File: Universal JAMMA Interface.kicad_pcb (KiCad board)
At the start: 2 copper layers, 111 x 60.8 mm, 31 parts, among them U1 LM386, U2 DIP-14_W7.62mm_Socket

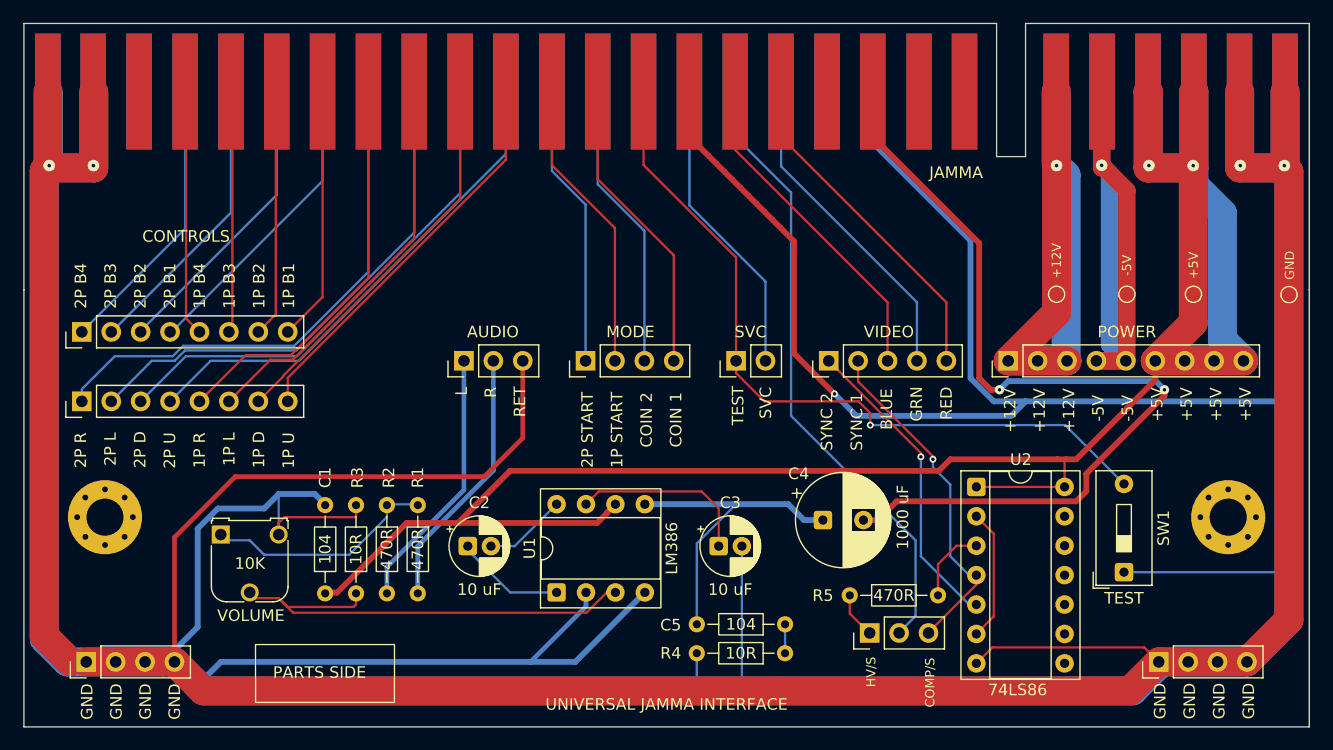
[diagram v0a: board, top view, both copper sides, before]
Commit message: Merge JAMMA/CHAMMA interfaces
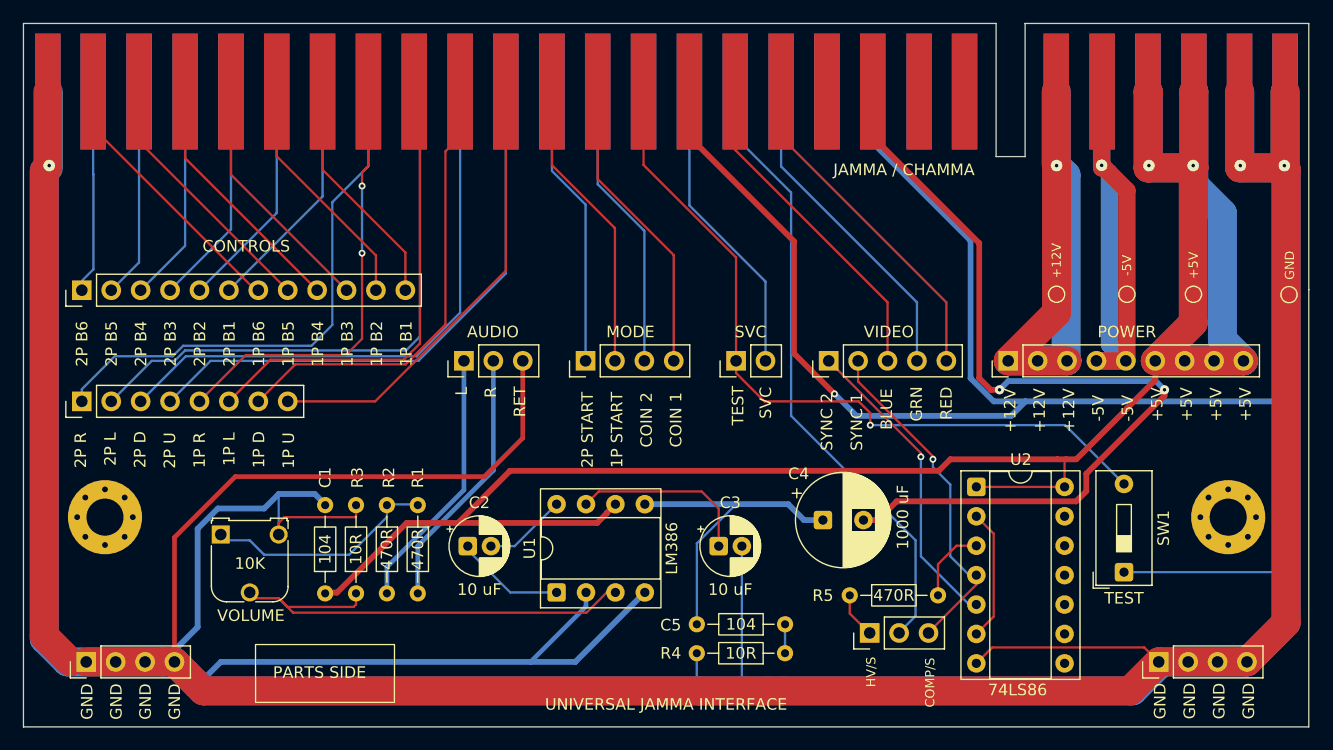
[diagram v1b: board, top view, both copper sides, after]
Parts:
- CONTROLS: value PinHeader_1x08_P2.54mm_Vertical -> PinHeader_1x12_P2.54mm_Vertical; footprint Connector_PinHeader_2.54mm:PinHeader_1x08_P2.54mm_Vertical -> Connector_PinHeader_2.54mm:PinHeader_1x12_P2.54mm_Vertical
- JAMMA / CHAMMA: renamed from JAMMA
- moved CONTROLS 3.60 mm to (99.0, 86.4)
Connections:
- CONTROLS pad 1: 2P_B4 -> 2P_B6
- CONTROLS pad 2: 2P_B3 -> 2P_B5
- CONTROLS pad 3: 2P_B2 -> 2P_B4
- CONTROLS pad 4: 2P_B1 -> 2P_B3
- CONTROLS pad 5: 1P_B4 -> 2P_B2
- CONTROLS pad 6: 1P_B3 -> 2P_B1
- CONTROLS pad 7: 1P_B2 -> 1P_B6
- CONTROLS pad 8: 1P_B1 -> 1P_B5
- JAMMA / CHAMMA pad 26: (no net) -> 1P_B5
- JAMMA / CHAMMA pad 27: GND -> 1P_B6
- JAMMA / CHAMMA pad d: (no net) -> 2P_B5
- JAMMA / CHAMMA pad e: GND -> 2P_B6
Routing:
- net 1P_B6: track 0.00 -> 23.2 mm
- net GND: track 746.4 -> 723.5 mm, vias 5 -> 4
- net 1P_B5: track 0.00 -> 22.5 mm
- net 2P_B5: track 0.00 -> 18.2 mm
- net 2P_B6: track 0.00 -> 17.6 mm
- net 2P_D: track 43.8 -> 49.9 mm
- net 2P_U: track 43.2 -> 49.3 mm
- net 1P_L: track 34.5 -> 40.5 mm
- net 2P_L: track 44.4 -> 50.3 mm
- net 2P_B4: track 24.5 -> 18.7 mm
- net 2P_B3: track 25.0 -> 19.3 mm
- net 2P_B1: track 26.2 -> 20.5 mm
- net 2P_B2: track 25.5 -> 19.9 mm
- net 1P_D: track 34.0 -> 39.6 mm
- net 1P_U: track 34.6 -> 39.0 mm
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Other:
- board text added: "1P B5"
- board text added: "1P B6"
- board text added: "2P B5"
- board text added: "2P B6"
